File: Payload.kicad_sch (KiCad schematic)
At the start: 11 parts, among them U1 STM32-(STM32H745ZIT6)

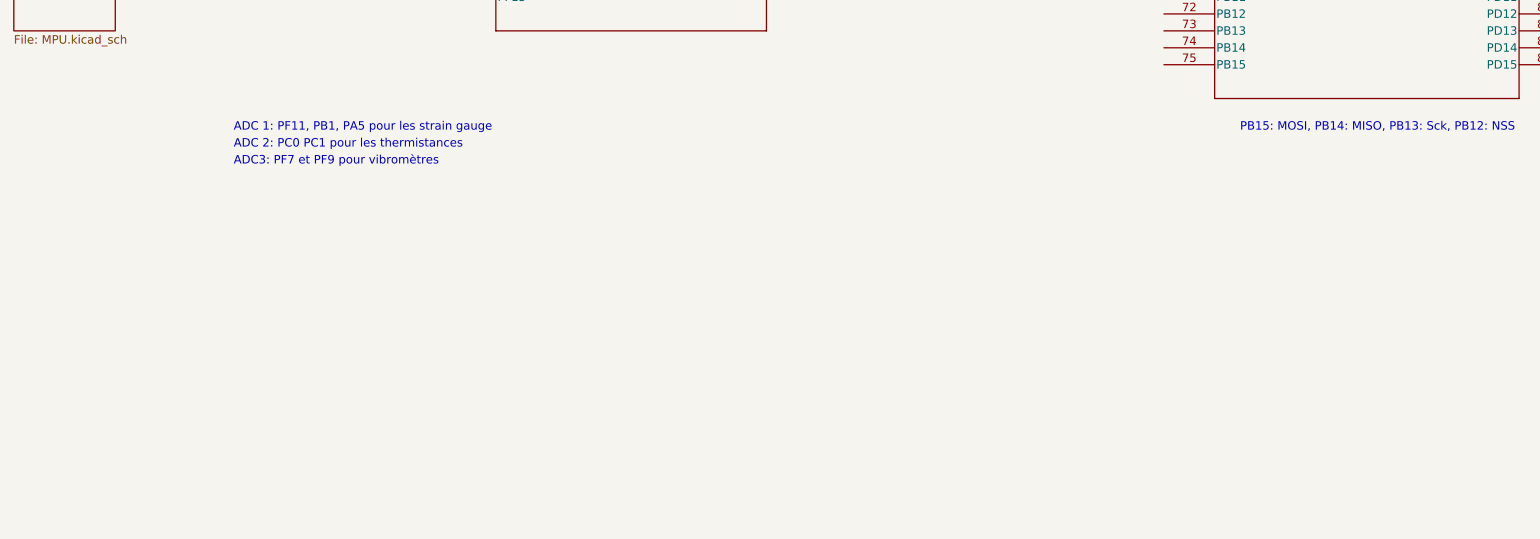
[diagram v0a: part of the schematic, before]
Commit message: Ajout de commentaires sur les pins inutilisés
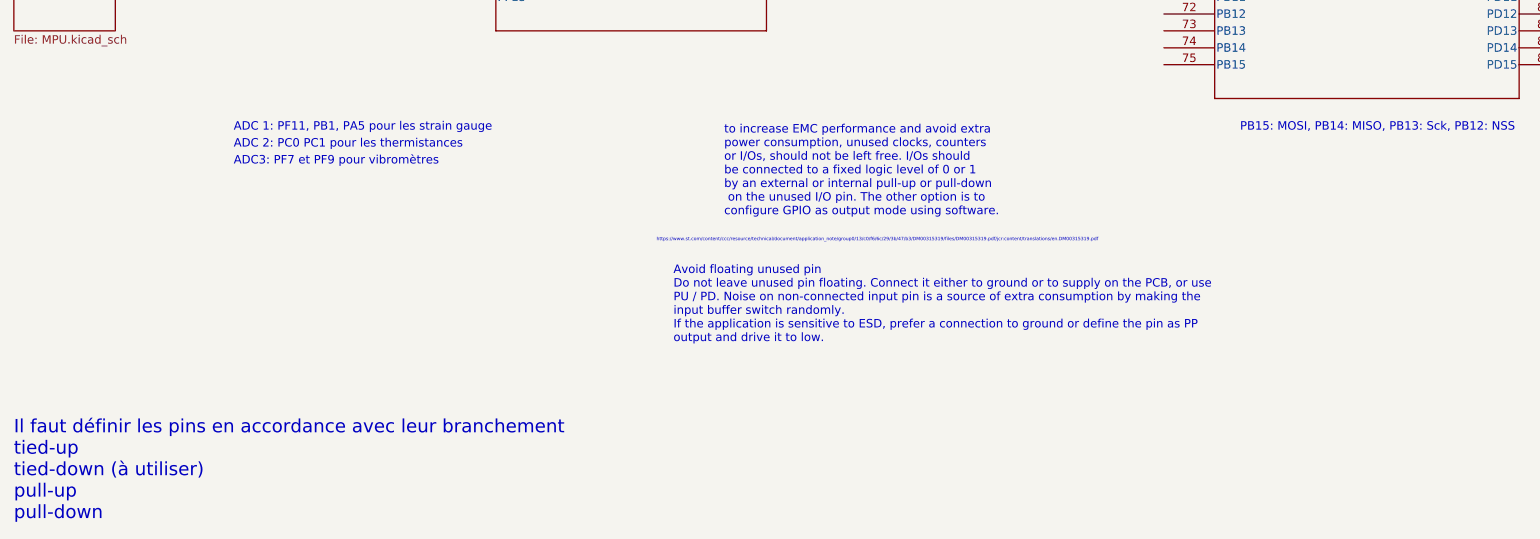
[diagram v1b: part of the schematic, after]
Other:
- note added: "Avoid floating unused pin Do not leave unused pin floating. Connect it either to ground or to supply on the PCB, or use PU / PD. Noise on non-connected input pin is a source of extra consumption by making the input buffer switch randomly. If the application is sensitive to ESD, prefer a connection to ground or define the pin as PP output and drive it to low."
- note added: "Il faut définir les pins en accordance avec leur branchement tied-up tied-down (à utiliser) pull-up pull-down"
- note added: "https://www.st.com/content/ccc/resource/technical/document/application_note/group0/13/c0/f6/6c/29/3b/47/b3/DM00315319/files/DM00315319.pdf/jcr:content/translations/en.DM00315319.pdf"
- note added: "to increase EMC performance and avoid extra power consumption, unused clocks, counters or I/Os, should not be left free. I/Os should be connected to a fixed logic level of 0 or 1 by an external or internal pull-up or pull-down on the unused I/O pin. The other option is to configure GPIO as output mode using software."
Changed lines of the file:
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@@
     (stroke (width 0) (type default))
+  )
+  (text "https://www.st.com/content/ccc/resource/technical/document/application_note/group0/13/c0/f6/6c/29/3b/47/b3/DM00315319/files/DM00315319.pdf/jcr:content/translations/en.DM00315319.pdf"
+    (at 113.03 142.24 0)
+    (effects (font (size 0.5 0.5) (color 255 0 226 1)) (justify left bottom))
   )
   (text "ADC3: PF7 et PF9 pour vibromètres" (at 49.53 130.81 0)
@@
     (effects (font (size 1.27 1.27)) (justify left bottom))
   )
+  (text "Il faut définir les pins en accordance avec leur branchement \ntied-up\ntied-down (à utiliser)\npull-up \npull-down"
+    (at 16.51 184.15 0)
+    (effects (font (size 2 2)) (justify left bottom))
+  )
+  (text "Avoid floating unused pin\nDo not leave unused pin floating. Connect it either to ground or to supply on the PCB, or use\nPU / PD. Noise on non-connected input pin is a source of extra consumption by making the\ninput buffer switch randomly.\nIf the application is sensitive to ESD, prefer a connection to ground or define the pin as PP\noutput and drive it to low.\n"
+    (at 115.57 157.48 0)
+    (effects (font (size 1.27 1.27)) (justify left bottom))
+  )
   (text "PB15: MOSI, PB14: MISO, PB13: Sck, PB12: NSS" (at 200.66 125.73 0)
+    (effects (font (size 1.27 1.27)) (justify left bottom))
+  )
+  (text "to increase EMC performance and avoid extra\npower consumption, unused clocks, counters \nor I/Os, should not be left free. I/Os should\nbe connected to a fixed logic level of 0 or 1\nby an external or internal pull-up or pull-down\n on the unused I/O pin. The other option is to \nconfigure GPIO as output mode using software."
+    (at 123.19 138.43 0)
     (effects (font (size 1.27 1.27)) (justify left bottom))
   )
@@
       (effects (font (size 1.27 1.27)) hide)
     )
-    (pin "2")
-    (pin "1")
+    (pin "1")
+    (pin "2")
     (instances
       (project "Payload"
@@
       (effects (font (size 1.27 1.27)) hide)
     )
-    (pin "2")
-    (pin "1")
+    (pin "1")
+    (pin "2")
     (instances
       (project "Payload"
@@
       (effects (font (size 1.27 1.27)) hide)
     )
-    (pin "2")
-    (pin "1")
+    (pin "1")
+    (pin "2")
     (instances
       (project "Payload"
@@
       (effects (font (size 1.27 1.27)) hide)
     )
-    (pin "2")
-    (pin "1")
+    (pin "1")
+    (pin "2")
     (instances
       (project "Payload"
@@
       (effects (font (size 1.27 1.27)) hide)
     )
-    (pin "2")
-    (pin "1")
+    (pin "1")
+    (pin "2")
     (instances
       (project "Payload"
@@
       (effects (font (size 1.27 1.27)) hide)
     )
-    (pin "2")
-    (pin "1")
+    (pin "1")
+    (pin "2")
     (instances
       (project "Payload"
@@
       (effects (font (size 1.27 1.27)) hide)
     )
-    (pin "2")
-    (pin "1")
-    (instances
-      (project "Payload"
+    (pin "1")
+    (pin "2")
+    (instances
+      (project "Payload"

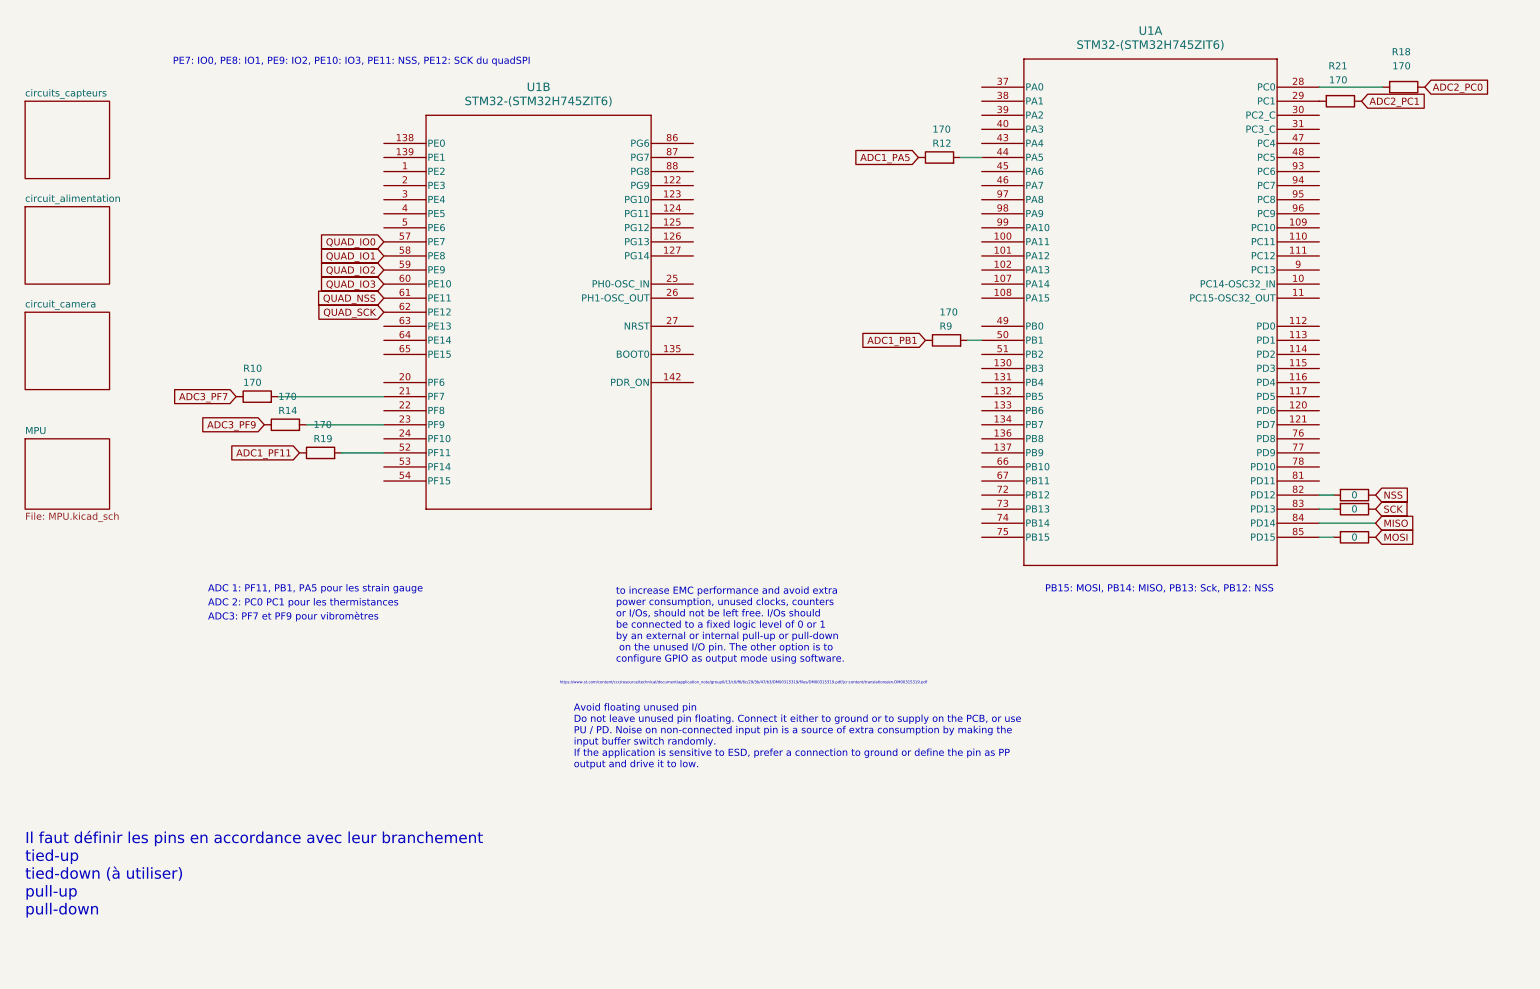
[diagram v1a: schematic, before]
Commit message: Groundé tous les GPIO du stm32
il manque juste le boot0 et une autre pin
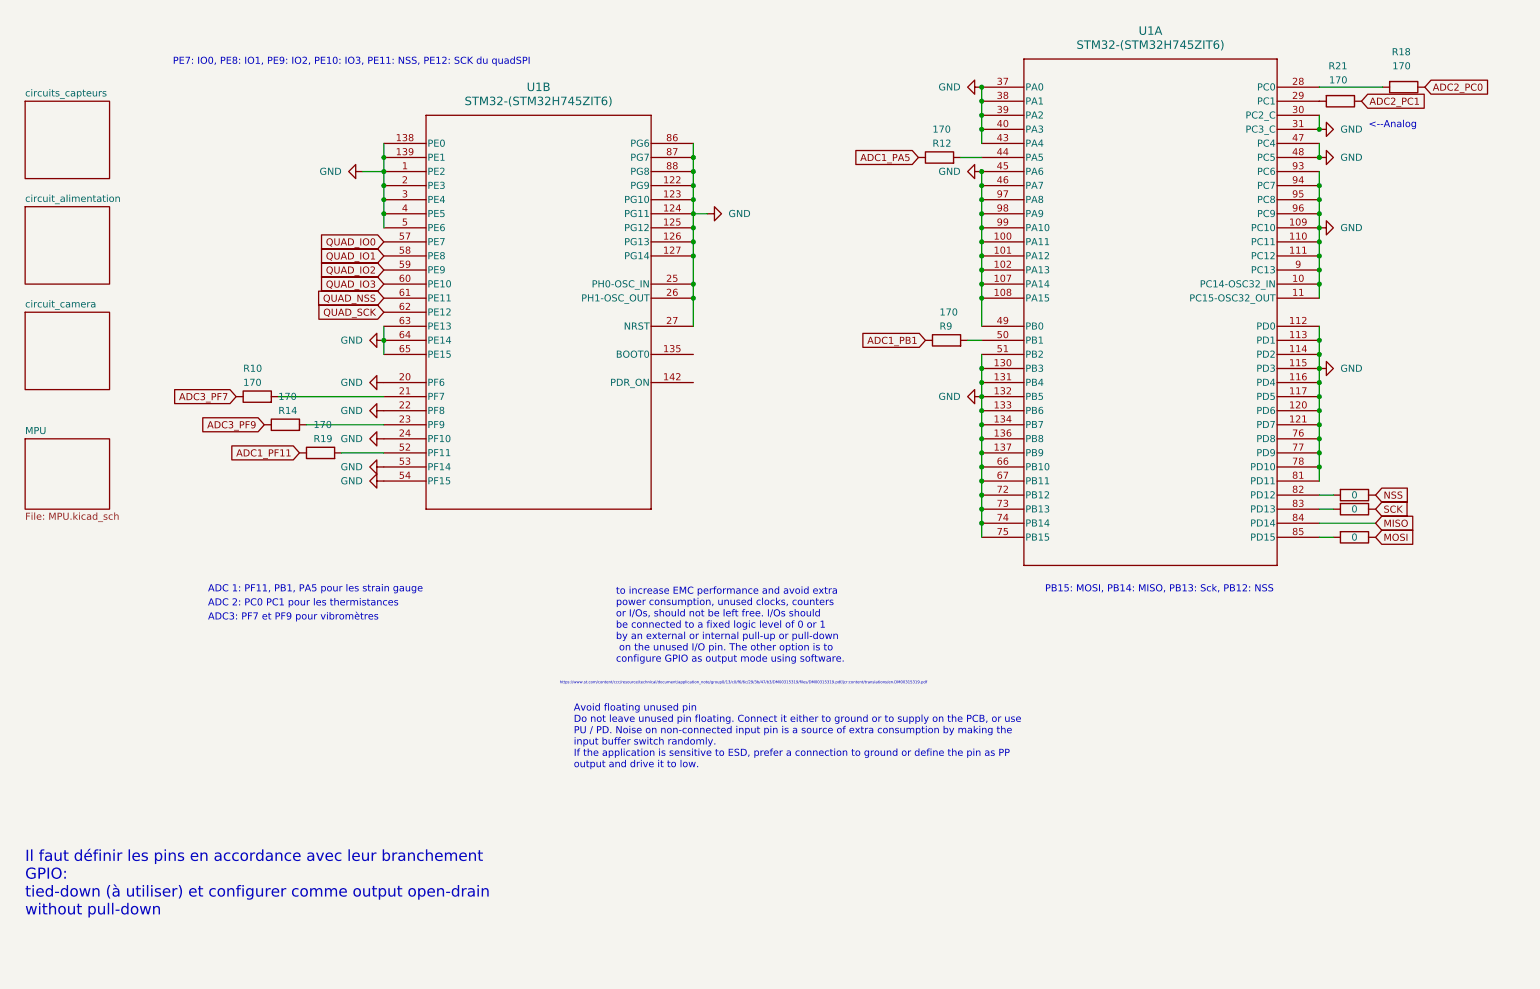
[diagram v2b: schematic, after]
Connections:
- net GND: now reaches U1.1 (PE2)
- net GND: now also U1.10 (PC14-OSC32_IN), U1.100 (PA11), U1.101 (PA12), U1.102 (PA13), U1.107 (PA14), U1.108 (PA15), U1.109 (PC10), U1.11 (PC15-OSC32_OUT), U1.110 (PC11), U1.111 (PC12), U1.112 (PD0), U1.113 (PD1), U1.114 (PD2), U1.115 (PD3), U1.116 (PD4), U1.117 (PD5), U1.120 (PD6), U1.121 (PD7), U1.122 (PG9), U1.123 (PG10), U1.124 (PG11), U1.125 (PG12), U1.126 (PG13), U1.127 (PG14), U1.130 (PB3), U1.131 (PB4), U1.132 (PB5), U1.133 (PB6), U1.134 (PB7), U1.136 (PB8), U1.137 (PB9), U1.138 (PE0), U1.139 (PE1), U1.2 (PE3), U1.20 (PF6), U1.22 (PF8), U1.24 (PF10), U1.25 (PH0-OSC_IN), U1.26 (PH1-OSC_OUT), U1.27 (NRST), U1.3 (PE4), U1.30 (PC2_C), U1.31 (PC3_C), U1.37 (PA0), U1.38 (PA1), U1.39 (PA2), U1.4 (PE5), U1.40 (PA3), U1.43 (PA4), U1.45 (PA6), U1.46 (PA7), U1.47 (PC4), U1.48 (PC5), U1.49 (PB0), U1.5 (PE6), U1.51 (PB2), U1.53 (PF14), U1.54 (PF15), U1.63 (PE13), U1.64 (PE14), U1.65 (PE15), U1.66 (PB10), U1.67 (PB11), U1.72 (PB12), U1.73 (PB13), U1.74 (PB14), U1.75 (PB15), U1.76 (PD8), U1.77 (PD9), U1.78 (PD10), U1.81 (PD11), U1.86 (PG6), U1.87 (PG7), U1.88 (PG8), U1.9 (PC13), U1.93 (PC6), U1.94 (PC7), U1.95 (PC8), U1.96 (PC9), U1.97 (PA8), U1.98 (PA9), U1.99 (PA10)
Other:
- note added: "<--Analog"
- note added: "Il faut définir les pins en accordance avec leur branchement GPIO: tied-down (à utiliser) et configurer comme output open-drain without pull-down"
- note removed: "Il faut définir les pins en accordance avec leur branchement tied-up tied-down (à utiliser) pull-up pull-down"

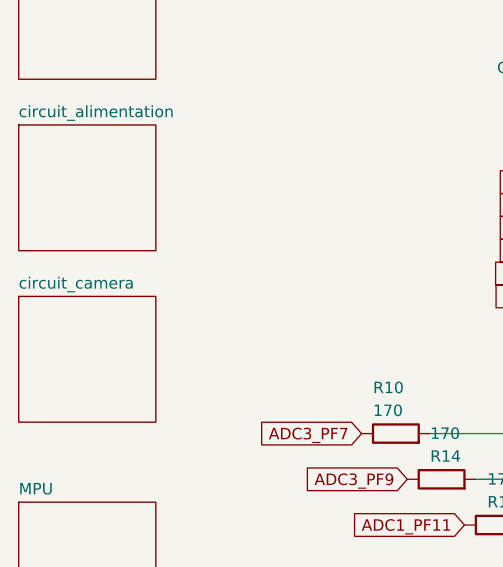
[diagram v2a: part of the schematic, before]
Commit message: Renommer circuit caméra à payload
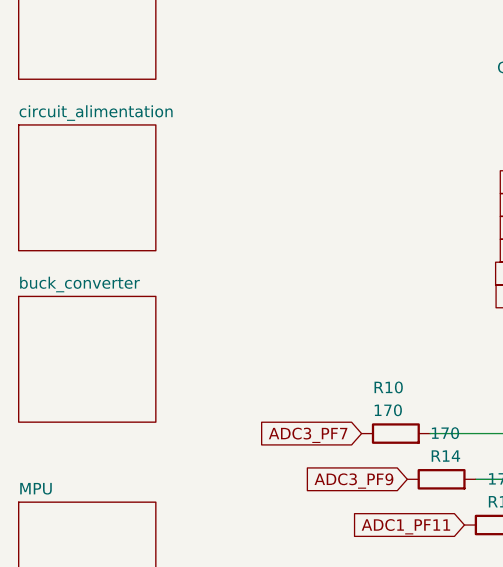
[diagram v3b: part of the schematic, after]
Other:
- sheet circuit_camera renamed buck_converter
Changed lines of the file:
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@@
     (stroke (width 0.1524) (type solid))
     (fill (color 0 0 0 0.0000))
-    (property "Sheetname" "circuit_camera" (at 16.51 74.2184 0)
+    (property "Sheetname" "buck_converter" (at 16.51 74.2184 0)
       (effects (font (size 1.27 1.27)) (justify left bottom))
     )

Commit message: Plein de modifs
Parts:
- added R25: 100 K, symbol Device:R
- added R26: 10K, symbol Device:R
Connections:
- net GND: now also U1.142 (PDR_ON), R26.2; no longer U1.102 (PA13), U1.107 (PA14), U1.130 (PB3), U1.27 (NRST)
- net at U1.135 (BOOT0): now also R26.1
- new net +3.3V: R25.1
- new net SWCLK: U1.107 (PA14)
- new net SWDIO: R25.2, U1.102 (PA13)
- new net SWO: U1.130 (PB3)
- no-connect marks 0 -> 1
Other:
- added sheet IO (IO.kicad_sch)

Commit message: Mémoire
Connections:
- net GND: no longer U1.100 (PA11), U1.101 (PA12), U1.99 (PA10)
- new net USB_D+: U1.101 (PA12)
- new net USB_D-: U1.100 (PA11)
- new net USB_check: U1.99 (PA10)
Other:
- note added: "internal pull up pin 101"
- moved on the sheet: R25
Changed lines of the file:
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@@
   (junction (at 189.23 107.95) (diameter 0) (color 0 0 0 0)
   )
+  (junction (at 165.1 67.31) (diameter 0) (color 0 0 0 0)
+  )
   (junction (at 81.28 46.99) (diameter 0) (color 0 0 0 0)
   )
@@
   (junction (at 250.19 52.07) (diameter 0) (color 0 0 0 0)
   )
-  (junction (at 189.23 59.69) (diameter 0) (color 0 0 0 0)
-  )
   (junction (at 81.28 80.01) (diameter 0) (color 0 0 0 0)
   )
@@
   (junction (at 189.23 100.33) (diameter 0) (color 0 0 0 0)
   )
-  (junction (at 176.53 67.31) (diameter 0) (color 0 0 0 0)
-  )
   (junction (at 189.23 113.03) (diameter 0) (color 0 0 0 0)
   )
@@
   (junction (at 189.23 54.61) (diameter 0) (color 0 0 0 0)
   )
-  (junction (at 189.23 62.23) (diameter 0) (color 0 0 0 0)
-  )
   (junction (at 81.28 52.07) (diameter 0) (color 0 0 0 0)
   )
@@
   )
   (junction (at 250.19 54.61) (diameter 0) (color 0 0 0 0)
-  )
-  (junction (at 189.23 57.15) (diameter 0) (color 0 0 0 0)
   )
   (junction (at 250.19 64.77) (diameter 0) (color 0 0 0 0)
@@
     (stroke (width 0) (type default))
   )
-  (wire (pts (xy 189.23 59.69) (xy 189.23 62.23))
-    (stroke (width 0) (type default))
-  )
   (wire (pts (xy 189.23 95.25) (xy 189.23 97.79))
     (stroke (width 0) (type default))
@@
     (stroke (width 0) (type default))
   )
-  (wire (pts (xy 171.45 67.31) (xy 176.53 67.31))
+  (wire (pts (xy 162.56 67.31) (xy 165.1 67.31))
     (stroke (width 0) (type default))
   )
@@
     (stroke (width 0) (type default))
   )
-  (wire (pts (xy 189.23 62.23) (xy 189.23 64.77))
-    (stroke (width 0) (type default))
-  )
   (wire (pts (xy 250.19 44.45) (xy 250.19 46.99))
     (stroke (width 0) (type default))
@@
     (stroke (width 0) (type default))
   )
-  (wire (pts (xy 189.23 57.15) (xy 189.23 59.69))
-    (stroke (width 0) (type default))
-  )
   (wire (pts (xy 250.19 107.95) (xy 252.73 107.95))
     (stroke (width 0) (type default))
@@
     (stroke (width 0) (type default))
   )
-  (wire (pts (xy 176.53 67.31) (xy 189.23 67.31))
+  (wire (pts (xy 165.1 67.31) (xy 189.23 67.31))
     (stroke (width 0) (type default))
   )
@@
   (wire (pts (xy 189.23 110.49) (xy 189.23 113.03))
     (stroke (width 0) (type default))
+  )
+  (text "internal pull up pin 101" (at 204.47 64.77 0)
+    (effects (font (size 1.27 1.27)) (justify left bottom))
   )
   (text "https://www.st.com/content/ccc/resource/technical/document/application_note/group0/13/c0/f6/6c/29/3b/47/b3/DM00315319/files/DM00315319.pdf/jcr:content/translations/en.DM00315319.pdf"
@@
     )
   )
-  (global_label "SWDIO" (shape input) (at 171.45 67.31 180) (fields_autoplaced)
-    (effects (font (size 1.27 1.27)) (justify right))
-    (property "Intersheetrefs" "${INTERSHEET_REFS}" (at 162.5986 67.31 0)
+  (global_label "SWDIO" (shape input) (at 162.56 67.31 180) (fields_autoplaced)
+    (effects (font (size 1.27 1.27)) (justify right))
+    (property "Intersheetrefs" "${INTERSHEET_REFS}" (at 153.7086 67.31 0)
       (effects (font (size 1.27 1.27)) (justify right) hide)
     )
@@
     )
   )
+  (global_label "USB_D+" (shape input) (at 189.23 64.77 180) (fields_autoplaced)
+    (effects (font (size 1.27 1.27)) (justify right))
+    (property "Intersheetrefs" "${INTERSHEET_REFS}" (at 178.6248 64.77 0)
+      (effects (font (size 1.27 1.27)) (justify right) hide)
+    )
+  )
+  (global_label "USB_check" (shape input) (at 189.23 59.69 180) (fields_autoplaced)
+    (effects (font (size 1.27 1.27)) (justify right))
+    (property "Intersheetrefs" "${INTERSHEET_REFS}" (at 176.0243 59.69 0)
+      (effects (font (size 1.27 1.27)) (justify right) hide)
+    )
+  )
+  (global_label "USB_D-" (shape input) (at 189.23 62.23 180) (fields_autoplaced)
+    (effects (font (size 1.27 1.27)) (justify right))
+    (property "Intersheetrefs" "${INTERSHEET_REFS}" (at 178.6248 62.23 0)
+      (effects (font (size 1.27 1.27)) (justify right) hide)
+    )
+  )
   (global_label "QUAD_IO1" (shape input) (at 81.28 64.77 180) (fields_autoplaced)
     (effects (font (size 1.27 1.27)) (justify right))
@@
     )
   )
-  (symbol (lib_id "Device:R") (at 176.53 63.5 0) (unit 1)
-    (in_bom yes) (on_board yes) (dnp no) (fields_autoplaced)
-    (property "Reference" "R25" (at 179.07 62.23 0)
+  (symbol (lib_id "Device:R") (at 165.1 63.5 0) (unit 1)
+    (in_bom yes) (on_board yes) (dnp no) (fields_autoplaced)
+    (property "Reference" "R25" (at 167.64 62.23 0)
       (effects (font (size 1.27 1.27)) (justify left))
     )
-    (property "Value" "100 K" (at 179.07 64.77 0)
+    (property "Value" "100 K" (at 167.64 64.77 0)
       (effects (font (size 1.27 1.27)) (justify left))
     )
-    (property "Footprint" "" (at 174.752 63.5 90)
-      (effects (font (size 1.27 1.27)) hide)
-    )
-    (property "Datasheet" "~" (at 176.53 63.5 0)
+    (property "Footprint" "" (at 163.322 63.5 90)
+      (effects (font (size 1.27 1.27)) hide)
+    )
+    (property "Datasheet" "~" (at 165.1 63.5 0)
       (effects (font (size 1.27 1.27)) hide)
     )
@@
     )
   )
-  (symbol (lib_id "power:+3.3V") (at 176.53 59.69 0) (unit 1)
-    (in_bom yes) (on_board yes) (dnp no) (fields_autoplaced)
-    (property "Reference" "#PWR0101" (at 176.53 63.5 0)
-      (effects (font (size 1.27 1.27)) hide)
-    )
-    (property "Value" "+3.3V" (at 176.53 54.61 0)
+  (symbol (lib_id "power:+3.3V") (at 165.1 59.69 0) (unit 1)
+    (in_bom yes) (on_board yes) (dnp no) (fields_autoplaced)
+    (property "Reference" "#PWR0101" (at 165.1 63.5 0)
+      (effects (font (size 1.27 1.27)) hide)
+    )
+    (property "Value" "+3.3V" (at 165.1 54.61 0)
       (effects (font (size 1.27 1.27)))
     )
-    (property "Footprint" "" (at 176.53 59.69 0)
-      (effects (font (size 1.27 1.27)) hide)
-    )
-    (property "Datasheet" "" (at 176.53 59.69 0)
-      (effects (font (size 1.27 1.27)) hide)
-    )
+    (property "Footprint" "" (at 165.1 59.69 0)
+      (effects (font (size 1.27 1.27)) hide)
+    )
+    (property "Datasheet" "" (at 165.1 59.69 0)
+      (effects (font (size 1.27 1.27)) hide)
+    )
